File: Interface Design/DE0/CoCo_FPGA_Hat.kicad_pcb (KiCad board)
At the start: 2 copper layers, 53.3 x 44.5 mm, 18 parts, among them J1 J1, P1 CoCo_Slot, U1 74LVC245A, U2 74LVC245A, U3 74LVC245A, U4 74LVC245A

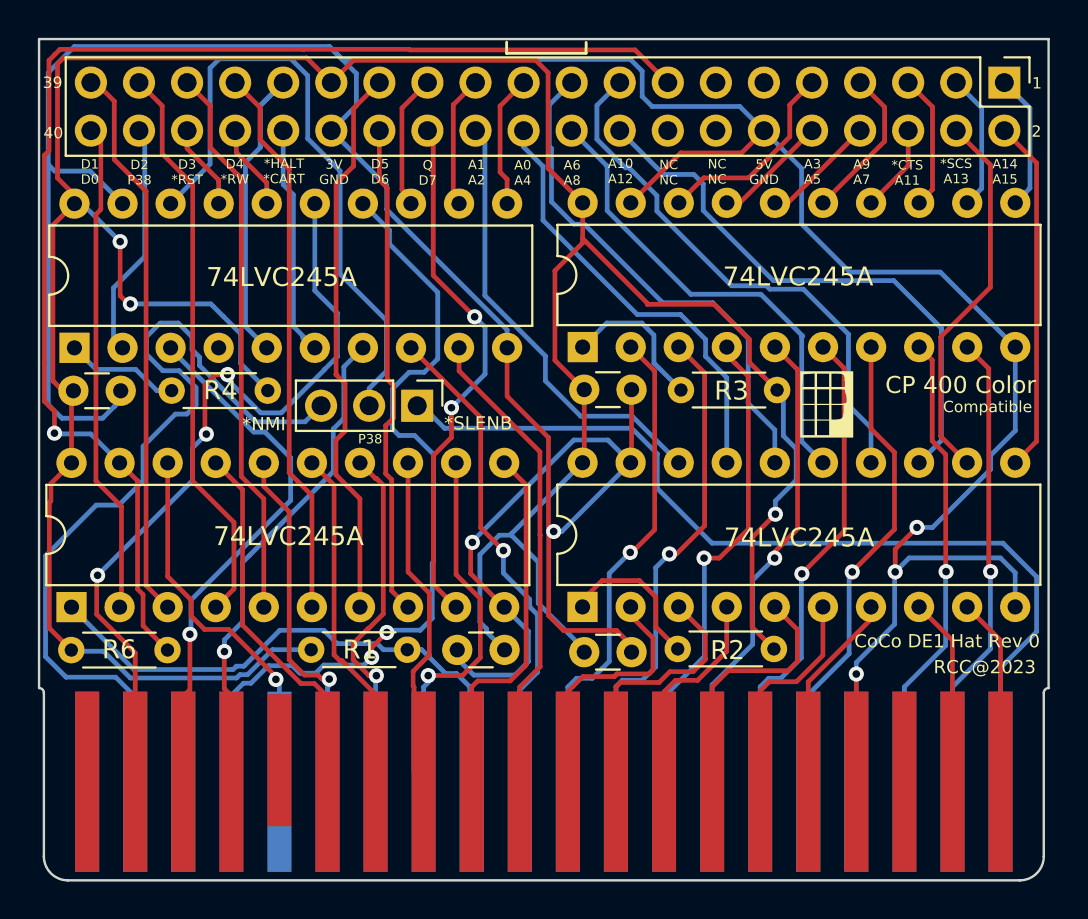
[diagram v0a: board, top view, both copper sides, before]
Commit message: REvised PCB for CoCo, added DE0 version
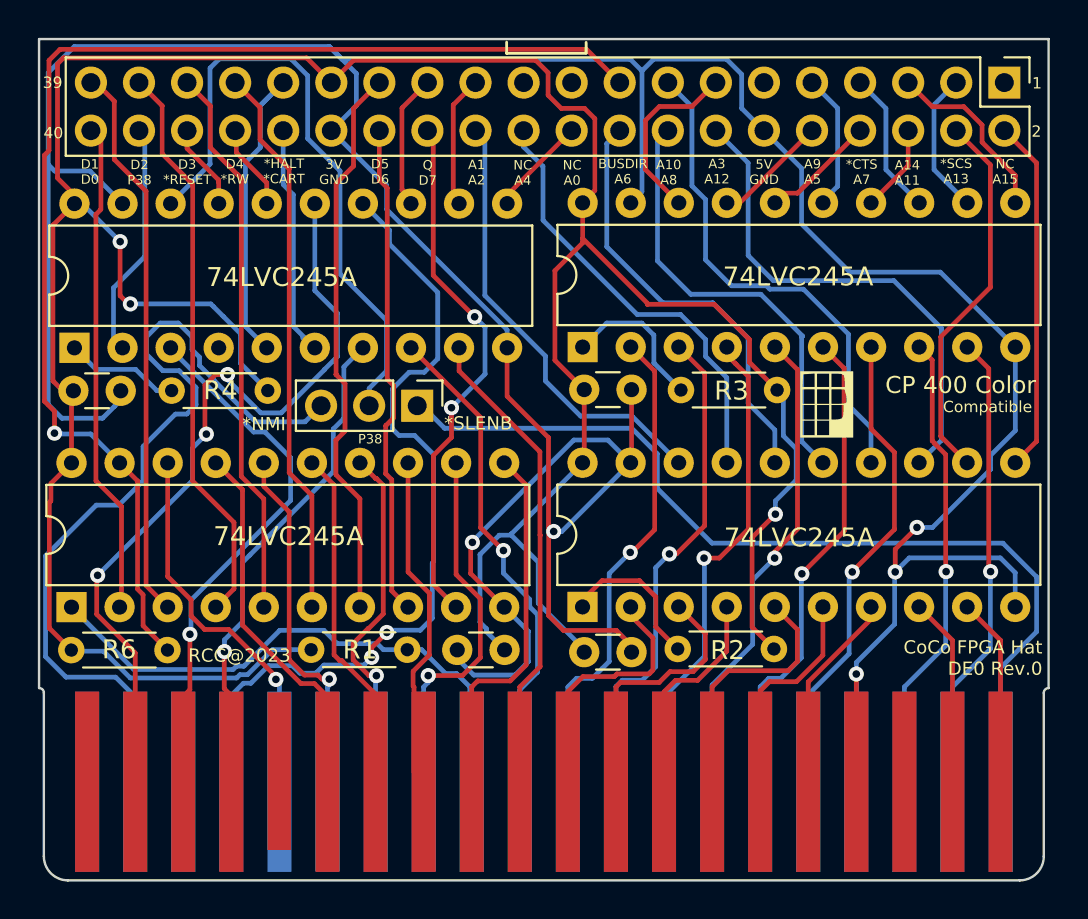
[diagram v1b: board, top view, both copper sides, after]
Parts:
- IDC1: value DE1 GPIO -> DE0 GPIO
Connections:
- IDC1 pad 1: C_A14 -> unconnected-(IDC1-Pad1)
- IDC1 pad 13: unconnected-(IDC1-Pad13) -> C_A3
- IDC1 pad 14: unconnected-(IDC1-Pad14) -> C_A12
- IDC1 pad 15: /C_BUSDIR -> C_A10
- IDC1 pad 16: unconnected-(IDC1-Pad16) -> C_A8
- IDC1 pad 17: C_A10 -> /C_BUSDIR
- IDC1 pad 18: C_A12 -> C_A6
- IDC1 pad 19: C_A6 -> unconnected-(IDC1-Pad19)
- IDC1 pad 20: C_A8 -> C_A0
- IDC1 pad 21: C_A0 -> unconnected-(IDC1-Pad21)
- IDC1 pad 5: *C_CTS -> C_A14
- IDC1 pad 7: C_A9 -> *C_CTS
- IDC1 pad 9: C_A3 -> C_A9
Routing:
- net C_A6: track 27.4 -> 23.1 mm
- net C_A12: track 29.7 -> 26.7 mm
- net /C_BUSDIR: track 68.7 -> 66.2 mm
- net C_A14: track 7.24 -> 9.67 mm
- net C_A10: track 28.8 -> 26.7 mm
- net C_A0: track 7.07 -> 5.27 mm
- net C_A8: track 25.3 -> 23.6 mm
- net Vdd: track 165.0 -> 166.2 mm
- net C_A3: track 10.7 -> 9.63 mm
- net C_A9: track 8.24 -> 7.24 mm
- net GNDREF: track 212.7 -> 212.1 mm
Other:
- board text added: "*CTS A7"
- board text added: "A10 A8"
- board text added: "A14 A11"
- board text added: "A3 A12"
- board text added: "A9 A5"
- board text added: "BUSDIR A6"
- board text added: "CoCo FPGA Hat DE0 Rev.0"
- board text added: "D3 *RESET"
- board text added: "NC A0"
- board text added: "NC A15"
- board text added: "NC A4"
- board text added: "https://github.com/costarc/CoCo_FPGA_Hat"
- board text removed: "*CTS A11"
- board text removed: "A0 A4"
- board text removed: "A10 A12"
- board text removed: "A14 A15"
- board text removed: "A3 A5"
- board text removed: "A6 A8"
- board text removed: "A9 A7"
- board text removed: "CoCo DE1 Hat Rev 0"
- board text removed: "D3 *RST"
- board text removed: "NC NC"
- board text removed: "https://github.com/costarc/CoCo_DE1_Hat"

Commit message: Added gerber files
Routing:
- net *NMI: track 45.7 -> 35.7 mm
- net *RESET: track 28.3 -> 24.2 mm, vias 1 -> 3
- net /C_BUSDIR: track 66.2 -> 69.1 mm
- net Q: track 26.1 -> 28.6 mm
- net *HALT: track 42.3 -> 43.1 mm, vias 3 -> 1
- added copper zone on B.Cu, net GNDREF
